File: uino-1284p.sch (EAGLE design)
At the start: 61 parts, among them J1 Micro USB, J2 M03X2, J3 CON_TERMINAL_BLOCK_02-5MM, J4 M03X2, J5 IO, Q1 MMBF0202PLT1, U1 ATMEGA8U2AU, U2 LD117AS50TR, U3 ATMEGA1284AU, X1 16MHz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

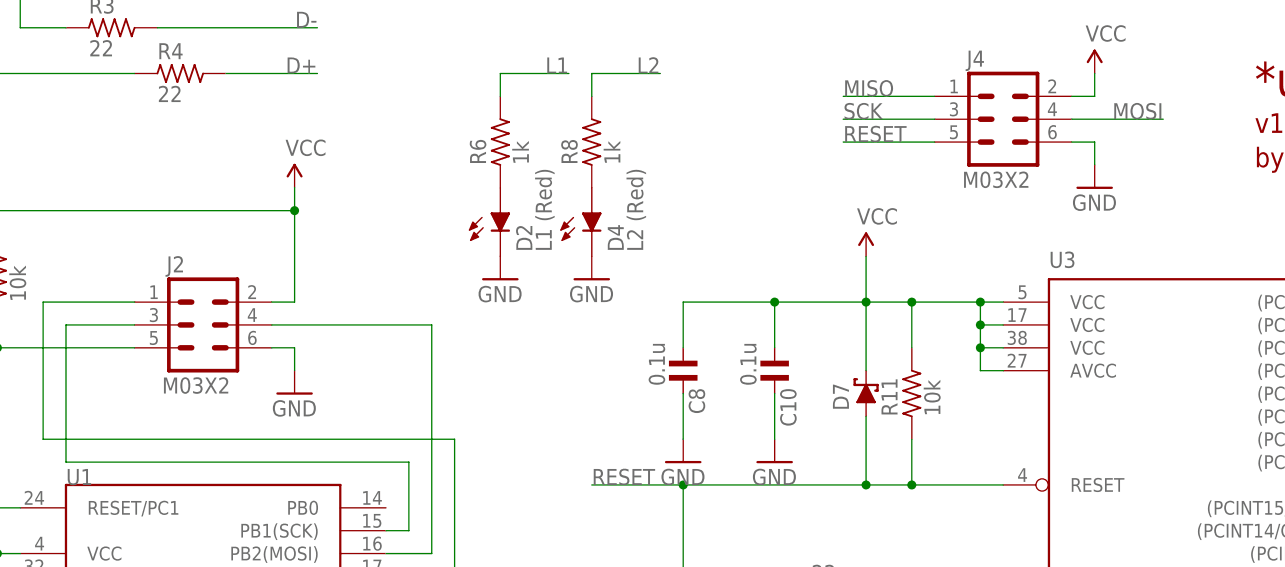
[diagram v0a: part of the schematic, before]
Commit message: Changed ISP header to offset style making use of permanent header optional (hopefully).
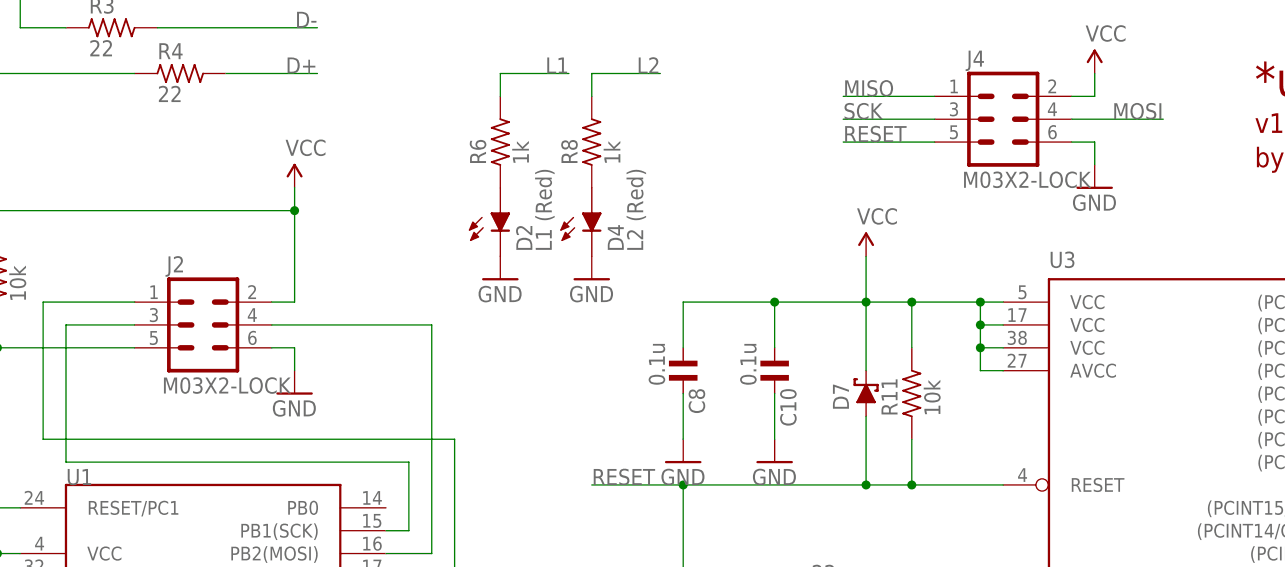
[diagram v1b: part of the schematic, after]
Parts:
- J2, J4: value M03X2 -> M03X2-LOCK; device adi-misc:M03X2 -> adi-misc:M03X2-LOCK
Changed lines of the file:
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@@
 <grid distance="0.1" unitdist="inch" unit="inch" style="lines" multiple="1" display="no" altdistance="0.01" altunitdist="inch" altunit="inch"/>
 <layers>
-<layer number="1" name="Top" color="4" fill="1" visible="no" active="no"/>
-<layer number="16" name="Bottom" color="1" fill="1" visible="no" active="no"/>
-<layer number="17" name="Pads" color="2" fill="1" visible="no" active="no"/>
-<layer number="18" name="Vias" color="2" fill="1" visible="no" active="no"/>
-<layer number="19" name="Unrouted" color="6" fill="1" visible="no" active="no"/>
-<layer number="20" name="Dimension" color="7" fill="1" visible="no" active="no"/>
-<layer number="21" name="tPlace" color="16" fill="1" visible="no" active="no"/>
-<layer number="22" name="bPlace" color="14" fill="1" visible="no" active="no"/>
-<layer number="23" name="tOrigins" color="15" fill="1" visible="no" active="no"/>
-<layer number="24" name="bOrigins" color="15" fill="1" visible="no" active="no"/>
-<layer number="25" name="tNames" color="7" fill="1" visible="no" active="no"/>
-<layer number="26" name="bNames" color="7" fill="1" visible="no" active="no"/>
-<layer number="27" name="tValues" color="7" fill="1" visible="no" active="no"/>
-<layer number="28" name="bValues" color="7" fill="1" visible="no" active="no"/>
+<layer number="1" name="Top" color="4" fill="1" visible="yes" active="no"/>
+<layer number="16" name="Bottom" color="1" fill="1" visible="yes" active="no"/>
+<layer number="17" name="Pads" color="2" fill="1" visible="yes" active="no"/>
+<layer number="18" name="Vias" color="2" fill="1" visible="yes" active="no"/>
+<layer number="19" name="Unrouted" color="6" fill="1" visible="yes" active="no"/>
+<layer number="20" name="Dimension" color="15" fill="1" visible="yes" active="no"/>
+<layer number="21" name="tPlace" color="7" fill="1" visible="yes" active="no"/>
+<layer number="22" name="bPlace" color="7" fill="1" visible="yes" active="no"/>
+<layer number="23" name="tOrigins" color="15" fill="1" visible="yes" active="no"/>
+<layer number="24" name="bOrigins" color="15" fill="1" visible="yes" active="no"/>
+<layer number="25" name="tNames" color="7" fill="1" visible="yes" active="no"/>
+<layer number="26" name="bNames" color="7" fill="1" visible="yes" active="no"/>
+<layer number="27" name="tValues" color="7" fill="1" visible="yes" active="no"/>
+<layer number="28" name="bValues" color="7" fill="1" visible="yes" active="no"/>
 <layer number="29" name="tStop" color="7" fill="3" visible="no" active="no"/>
 <layer number="30" name="bStop" color="7" fill="6" visible="no" active="no"/>
-<layer number="31" name="tCream" color="11" fill="4" visible="no" active="no"/>
+<layer number="31" name="tCream" color="7" fill="4" visible="no" active="no"/>
 <layer number="32" name="bCream" color="7" fill="5" visible="no" active="no"/>
 <layer number="33" name="tFinish" color="6" fill="3" visible="no" active="no"/>
@@
 <layer number="35" name="tGlue" color="7" fill="4" visible="no" active="no"/>
 <layer number="36" name="bGlue" color="7" fill="5" visible="no" active="no"/>
-<layer number="37" name="tTest" color="7" fill="1" visible="no" active="no"/>
-<layer number="38" name="bTest" color="7" fill="1" visible="no" active="no"/>
+<layer number="37" name="tTest" color="7" fill="1" visible="yes" active="no"/>
+<layer number="38" name="bTest" color="7" fill="1" visible="yes" active="no"/>
 <layer number="39" name="tKeepout" color="4" fill="11" visible="no" active="no"/>
 <layer number="40" name="bKeepout" color="1" fill="11" visible="no" active="no"/>
@@
 <layer number="44" name="Drills" color="7" fill="1" visible="no" active="no"/>
 <layer number="45" name="Holes" color="7" fill="1" visible="no" active="no"/>
-<layer number="46" name="Milling" color="3" fill="1" visible="no" active="no"/>
-<layer number="47" name="Measures" color="7" fill="1" visible="no" active="no"/>
-<layer number="48" name="Document" color="7" fill="1" visible="no" active="no"/>
-<layer number="49" name="Reference" color="13" fill="1" visible="no" active="no"/>
-<layer number="50" name="dxf" color="7" fill="1" visible="no" active="no"/>
-<layer number="51" name="tDocu" color="14" fill="1" visible="no" active="no"/>
-<layer number="52" name="bDocu" color="7" fill="1" visible="no" active="no"/>
-<layer number="53" name="tGND_GNDA" color="7" fill="9" visible="no" active="no"/>
-<layer number="54" name="bGND_GNDA" color="1" fill="9" visible="no" active="no"/>
-<layer number="56" name="wert" color="7" fill="1" visible="no" active="no"/>
-<layer number="57" name="tCAD" color="7" fill="1" visible="no" active="no"/>
-<layer number="58" name="bCAD" color="11" fill="1" visible="no" active="no"/>
-<layer number="59" name="tCarbon" color="7" fill="1" visible="no" active="no"/>
-<layer number="60" name="bCarbon" color="7" fill="1" visible="no" active="no"/>
+<layer number="46" name="Milling" color="3" fill="1" visible="yes" active="no"/>
+<layer number="47" name="Measures" color="7" fill="1" visible="yes" active="no"/>
+<layer number="48" name="Document" color="7" fill="1" visible="yes" active="no"/>
+<layer number="49" name="Reference" color="7" fill="1" visible="yes" active="no"/>
+<layer number="50" name="dxf" color="12" fill="1" visible="yes" active="no"/>
+<layer number="51" name="tDocu" color="7" fill="1" visible="yes" active="no"/>
+<layer number="52" name="bDocu" color="7" fill="1" visible="yes" active="no"/>
+<layer number="53" name="tGND_GNDA" color="7" fill="1" visible="yes" active="no"/>
+<layer number="54" name="bGND_GNDA" color="7" fill="1" visible="yes" active="no"/>
+<layer number="56" name="wert" color="7" fill="1" visible="yes" active="no"/>
+<layer number="57" name="tCAD" color="7" fill="1" visible="yes" active="no"/>
+<layer number="58" name="bCAD" color="11" fill="1" visible="yes" active="no"/>
+<layer number="59" name="tCarbon" color="7" fill="1" visible="yes" active="no"/>
+<layer number="60" name="bCarbon" color="7" fill="1" visible="yes" active="no"/>
 <layer number="90" name="Modules" color="5" fill="1" visible="yes" active="yes"/>
 <layer number="91" name="Nets" color="2" fill="1" visible="yes" active="yes"/>
@@
 <part name="JP3" library="SparkFun" deviceset="M08" device="1X08" value="IOL"/>
 <part name="JP4" library="adilinden" deviceset="M10" device="1X10" value="IOH"/>
-<part name="J4" library="adi-misc" deviceset="M03X2" device="" value="M03X2"/>
+<part name="J4" library="adi-misc" deviceset="M03X2" device="-LOCK" value="M03X2-LOCK"/>
 <part name="J1" library="adi-misc" deviceset="USB_MICRO_B_2.0-TH" device="" value="Micro USB"/>
 <part name="GND31" library="supply1" deviceset="GND" device=""/>
@@
 <part name="C11" library="rc-master-smd" deviceset="C_" device="0805MP" value="22p"/>
 <part name="C12" library="rc-master-smd" deviceset="C_" device="0805MP" value="22p"/>
-<part name="J2" library="adi-misc" deviceset="M03X2" device="" value="M03X2"/>
+<part name="J2" library="adi-misc" deviceset="M03X2" device="-LOCK" value="M03X2-LOCK"/>
 <part name="C4" library="rc-master-smd" deviceset="C_" device="0805MP" value="1u"/>
 <part name="GND4" library="supply1" deviceset="GND" device=""/>

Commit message: Version 1.4.
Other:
- note added: "v1.4 2016/11/13"
- note removed: "v1.3 2016/11/07"
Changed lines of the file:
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@@
 <grid distance="0.1" unitdist="inch" unit="inch" style="lines" multiple="1" display="no" altdistance="0.01" altunitdist="inch" altunit="inch"/>
 <layers>
-<layer number="1" name="Top" color="4" fill="1" visible="yes" active="no"/>
-<layer number="16" name="Bottom" color="1" fill="1" visible="yes" active="no"/>
-<layer number="17" name="Pads" color="2" fill="1" visible="yes" active="no"/>
-<layer number="18" name="Vias" color="2" fill="1" visible="yes" active="no"/>
-<layer number="19" name="Unrouted" color="6" fill="1" visible="yes" active="no"/>
-<layer number="20" name="Dimension" color="15" fill="1" visible="yes" active="no"/>
-<layer number="21" name="tPlace" color="7" fill="1" visible="yes" active="no"/>
-<layer number="22" name="bPlace" color="7" fill="1" visible="yes" active="no"/>
-<layer number="23" name="tOrigins" color="15" fill="1" visible="yes" active="no"/>
-<layer number="24" name="bOrigins" color="15" fill="1" visible="yes" active="no"/>
-<layer number="25" name="tNames" color="7" fill="1" visible="yes" active="no"/>
-<layer number="26" name="bNames" color="7" fill="1" visible="yes" active="no"/>
-<layer number="27" name="tValues" color="7" fill="1" visible="yes" active="no"/>
-<layer number="28" name="bValues" color="7" fill="1" visible="yes" active="no"/>
+<layer number="1" name="Top" color="4" fill="1" visible="no" active="no"/>
+<layer number="16" name="Bottom" color="1" fill="1" visible="no" active="no"/>
+<layer number="17" name="Pads" color="2" fill="1" visible="no" active="no"/>
+<layer number="18" name="Vias" color="2" fill="1" visible="no" active="no"/>
+<layer number="19" name="Unrouted" color="6" fill="1" visible="no" active="no"/>
+<layer number="20" name="Dimension" color="15" fill="1" visible="no" active="no"/>
+<layer number="21" name="tPlace" color="7" fill="1" visible="no" active="no"/>
+<layer number="22" name="bPlace" color="7" fill="1" visible="no" active="no"/>
+<layer number="23" name="tOrigins" color="15" fill="1" visible="no" active="no"/>
+<layer number="24" name="bOrigins" color="15" fill="1" visible="no" active="no"/>
+<layer number="25" name="tNames" color="7" fill="1" visible="no" active="no"/>
+<layer number="26" name="bNames" color="7" fill="1" visible="no" active="no"/>
+<layer number="27" name="tValues" color="7" fill="1" visible="no" active="no"/>
+<layer number="28" name="bValues" color="7" fill="1" visible="no" active="no"/>
 <layer number="29" name="tStop" color="7" fill="3" visible="no" active="no"/>
 <layer number="30" name="bStop" color="7" fill="6" visible="no" active="no"/>
@@
 <layer number="35" name="tGlue" color="7" fill="4" visible="no" active="no"/>
 <layer number="36" name="bGlue" color="7" fill="5" visible="no" active="no"/>
-<layer number="37" name="tTest" color="7" fill="1" visible="yes" active="no"/>
-<layer number="38" name="bTest" color="7" fill="1" visible="yes" active="no"/>
+<layer number="37" name="tTest" color="7" fill="1" visible="no" active="no"/>
+<layer number="38" name="bTest" color="7" fill="1" visible="no" active="no"/>
 <layer number="39" name="tKeepout" color="4" fill="11" visible="no" active="no"/>
 <layer number="40" name="bKeepout" color="1" fill="11" visible="no" active="no"/>
@@
 <layer number="44" name="Drills" color="7" fill="1" visible="no" active="no"/>
 <layer number="45" name="Holes" color="7" fill="1" visible="no" active="no"/>
-<layer number="46" name="Milling" color="3" fill="1" visible="yes" active="no"/>
-<layer number="47" name="Measures" color="7" fill="1" visible="yes" active="no"/>
-<layer number="48" name="Document" color="7" fill="1" visible="yes" active="no"/>
-<layer number="49" name="Reference" color="7" fill="1" visible="yes" active="no"/>
-<layer number="50" name="dxf" color="12" fill="1" visible="yes" active="no"/>
-<layer number="51" name="tDocu" color="7" fill="1" visible="yes" active="no"/>
-<layer number="52" name="bDocu" color="7" fill="1" visible="yes" active="no"/>
-<layer number="53" name="tGND_GNDA" color="7" fill="1" visible="yes" active="no"/>
-<layer number="54" name="bGND_GNDA" color="7" fill="1" visible="yes" active="no"/>
-<layer number="56" name="wert" color="7" fill="1" visible="yes" active="no"/>
-<layer number="57" name="tCAD" color="7" fill="1" visible="yes" active="no"/>
-<layer number="58" name="bCAD" color="11" fill="1" visible="yes" active="no"/>
-<layer number="59" name="tCarbon" color="7" fill="1" visible="yes" active="no"/>
-<layer number="60" name="bCarbon" color="7" fill="1" visible="yes" active="no"/>
+<layer number="46" name="Milling" color="3" fill="1" visible="no" active="no"/>
+<layer number="47" name="Measures" color="7" fill="1" visible="no" active="no"/>
+<layer number="48" name="Document" color="7" fill="1" visible="no" active="no"/>
+<layer number="49" name="Reference" color="7" fill="1" visible="no" active="no"/>
+<layer number="50" name="dxf" color="12" fill="1" visible="no" active="no"/>
+<layer number="51" name="tDocu" color="7" fill="1" visible="no" active="no"/>
+<layer number="52" name="bDocu" color="7" fill="1" visible="no" active="no"/>
+<layer number="53" name="tGND_GNDA" color="7" fill="1" visible="no" active="no"/>
+<layer number="54" name="bGND_GNDA" color="7" fill="1" visible="no" active="no"/>
+<layer number="56" name="wert" color="7" fill="1" visible="no" active="no"/>
+<layer number="57" name="tCAD" color="7" fill="1" visible="no" active="no"/>
+<layer number="58" name="bCAD" color="11" fill="1" visible="no" active="no"/>
+<layer number="59" name="tCarbon" color="7" fill="1" visible="no" active="no"/>
+<layer number="60" name="bCarbon" color="7" fill="1" visible="no" active="no"/>
 <layer number="90" name="Modules" color="5" fill="1" visible="yes" active="yes"/>
 <layer number="91" name="Nets" color="2" fill="1" visible="yes" active="yes"/>
@@
 <plain>
 <text x="172.72" y="137.16" size="3.81" layer="94" ratio="18">*uino-1284p</text>
-<text x="172.72" y="133.096" size="2.1844" layer="94" ratio="12">v1.3 2016/11/07</text>
+<text x="172.72" y="133.096" size="2.1844" layer="94" ratio="12">v1.4 2016/11/13</text>
 <text x="172.72" y="129.286" size="2.1844" layer="94" ratio="12">by Adi Linden</text>
 </plain>
